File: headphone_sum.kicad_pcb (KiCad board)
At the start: 2 copper layers, 23.1 x 128.5 mm, 44 parts, among them J1 IN_L1, J2 IN_L2, J3 IN_R1, J4 IN_R2, J5 OUT_LR, J6 Eurorack Power, J7 Conn_01x03_Male, J8 Conn_01x02_Female, M3 Screw MountingHole_3.2mm_M3, M3 screw locked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

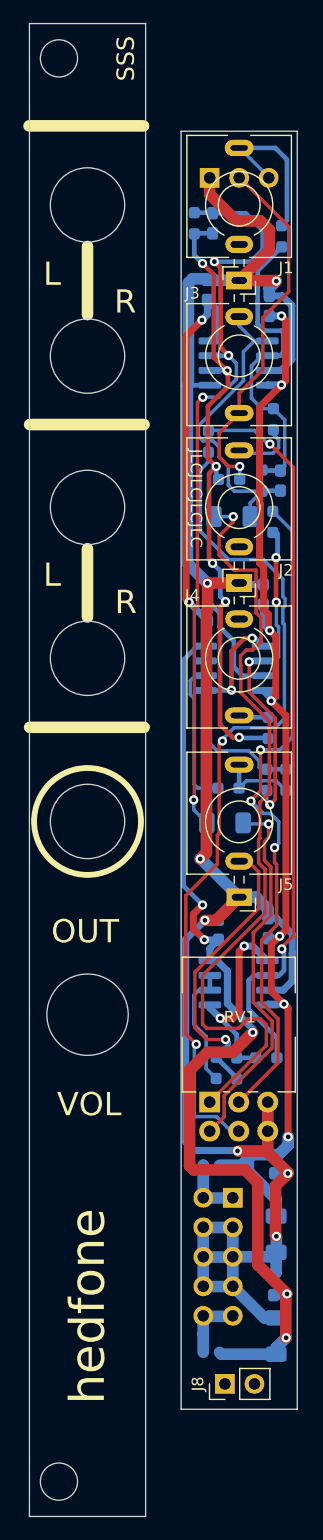
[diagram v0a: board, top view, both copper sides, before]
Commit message: Remove duplicate front/back file, old KiCad files.
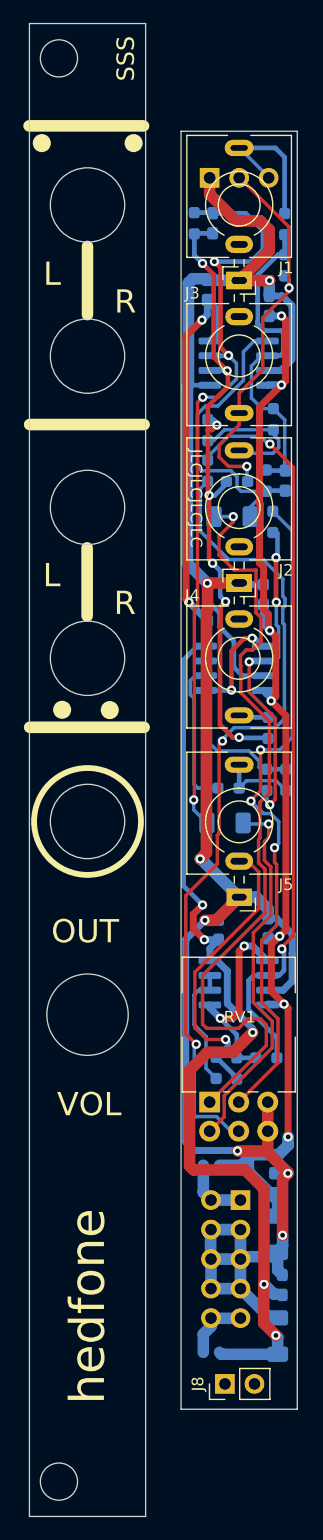
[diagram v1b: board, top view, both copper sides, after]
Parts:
- added R15: 200k, Resistor_SMD:R_0603_1608Metric_Pad0.98x0.95mm_HandSolder, B.Cu at (2.32, 25.7)
- added R16: 200k, Resistor_SMD:R_0603_1608Metric_Pad0.98x0.95mm_HandSolder, B.Cu at (8.94, 11.6)
- moved R4 2.50 mm to (2.32, 29.2)
- moved R1 1.07 mm to (8.94, 8.02)
- moved C5 0.74 mm to (8.74, 99.3)
- moved R5 0.70 mm to (4.84, 30.2)
- moved J6 0.69 mm to (5.14, 92.0)
- moved C12 0.41 mm to (8.99, 30.1)
- moved R8 0.36 mm to (7.37, 30.1)
- moved C3 0.13 mm to (8.34, 103.7)
- moved C4 0.13 mm to (8.34, 95.0)
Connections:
- J3 pad TN: Net-(C12-Pad2) -> unconnected-(J3-PadTN)
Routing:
- net Net-(J2-PadT): track 5.52 -> 11.6 mm
- net /R_POT_OUT: track 72.7 -> 70.2 mm
- net Net-(U1B--): track 54.4 -> 56.9 mm, vias 6 -> 7
- net R_IN: track 31.6 -> 33.9 mm, vias 1 -> 2
- net GND: track 194.0 -> 192.3 mm
- net Net-(U1A--): track 27.4 -> 28.9 mm
- net L_IN: track 14.1 -> 12.7 mm
- net Net-(U3A--): track 63.4 -> 64.4 mm
- net Net-(C12-Pad2): track 27.1 -> 26.3 mm
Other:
- board text added: "The J8 female pin header only connects to the back board, but is there to prevent the board flexing too much when inserting the power cable."
- board text added: "shedfönet"
- board text added: "v1.1"
- board text removed: "The J8 feamle pin header only connects to the back board, but is there to prevent the board flexing too much when inserting the power cable."
- board text removed: "v1.0"

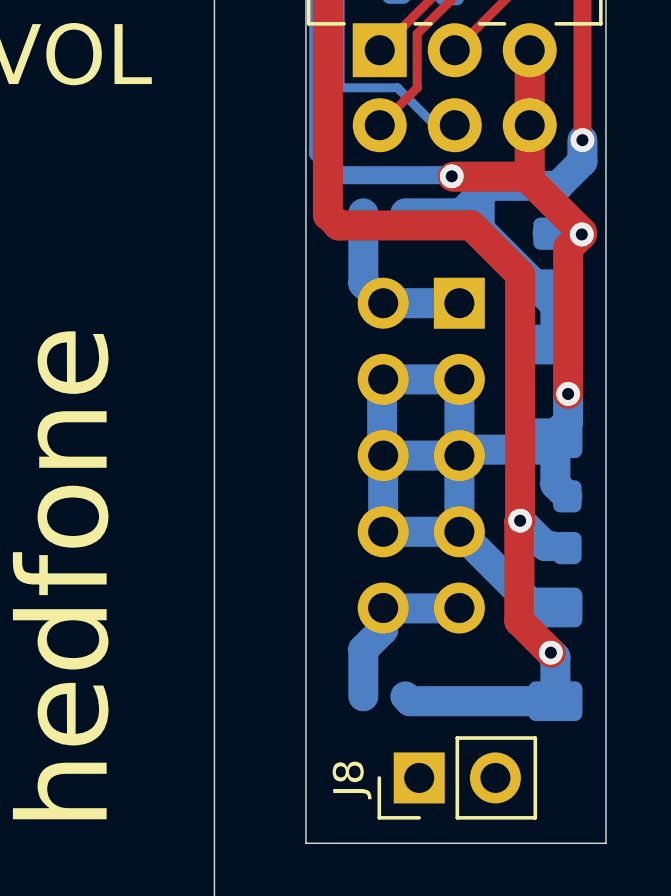
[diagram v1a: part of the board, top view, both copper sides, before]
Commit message: v1.1.1, fix some LCSC part numbers, fix D1,D2 footprint
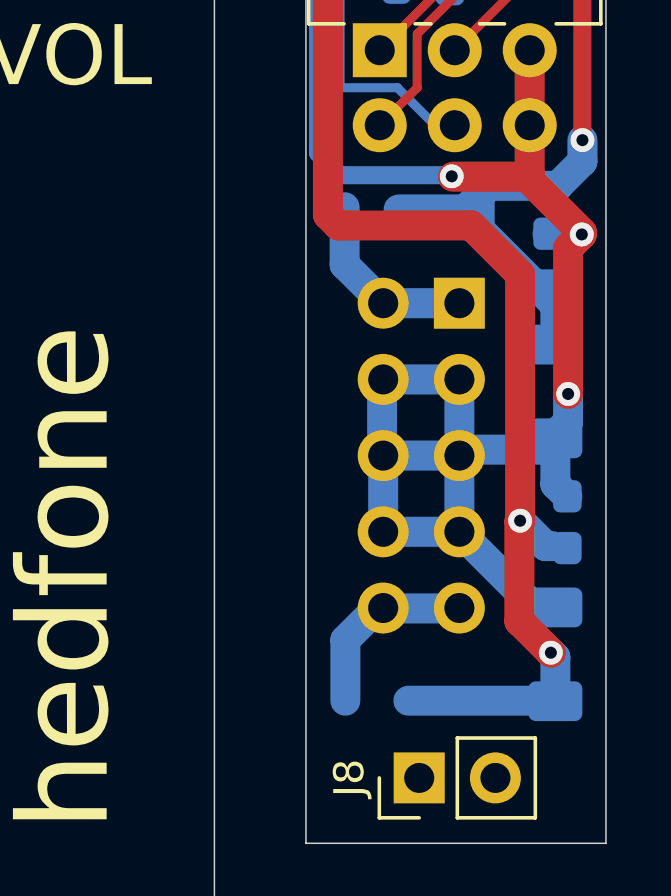
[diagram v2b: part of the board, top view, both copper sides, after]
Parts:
- D1, D2: footprint Diode_SMD:D_SOD-523 -> Diode_SMD:D_SOD-323
- moved D2 0.34 mm to (2.37, 88.8)
- moved D1 0.29 mm to (2.39, 105.3)
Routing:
- net Net-(D1-A): track 5.77 -> 6.28 mm
